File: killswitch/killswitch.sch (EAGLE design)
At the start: 12 parts

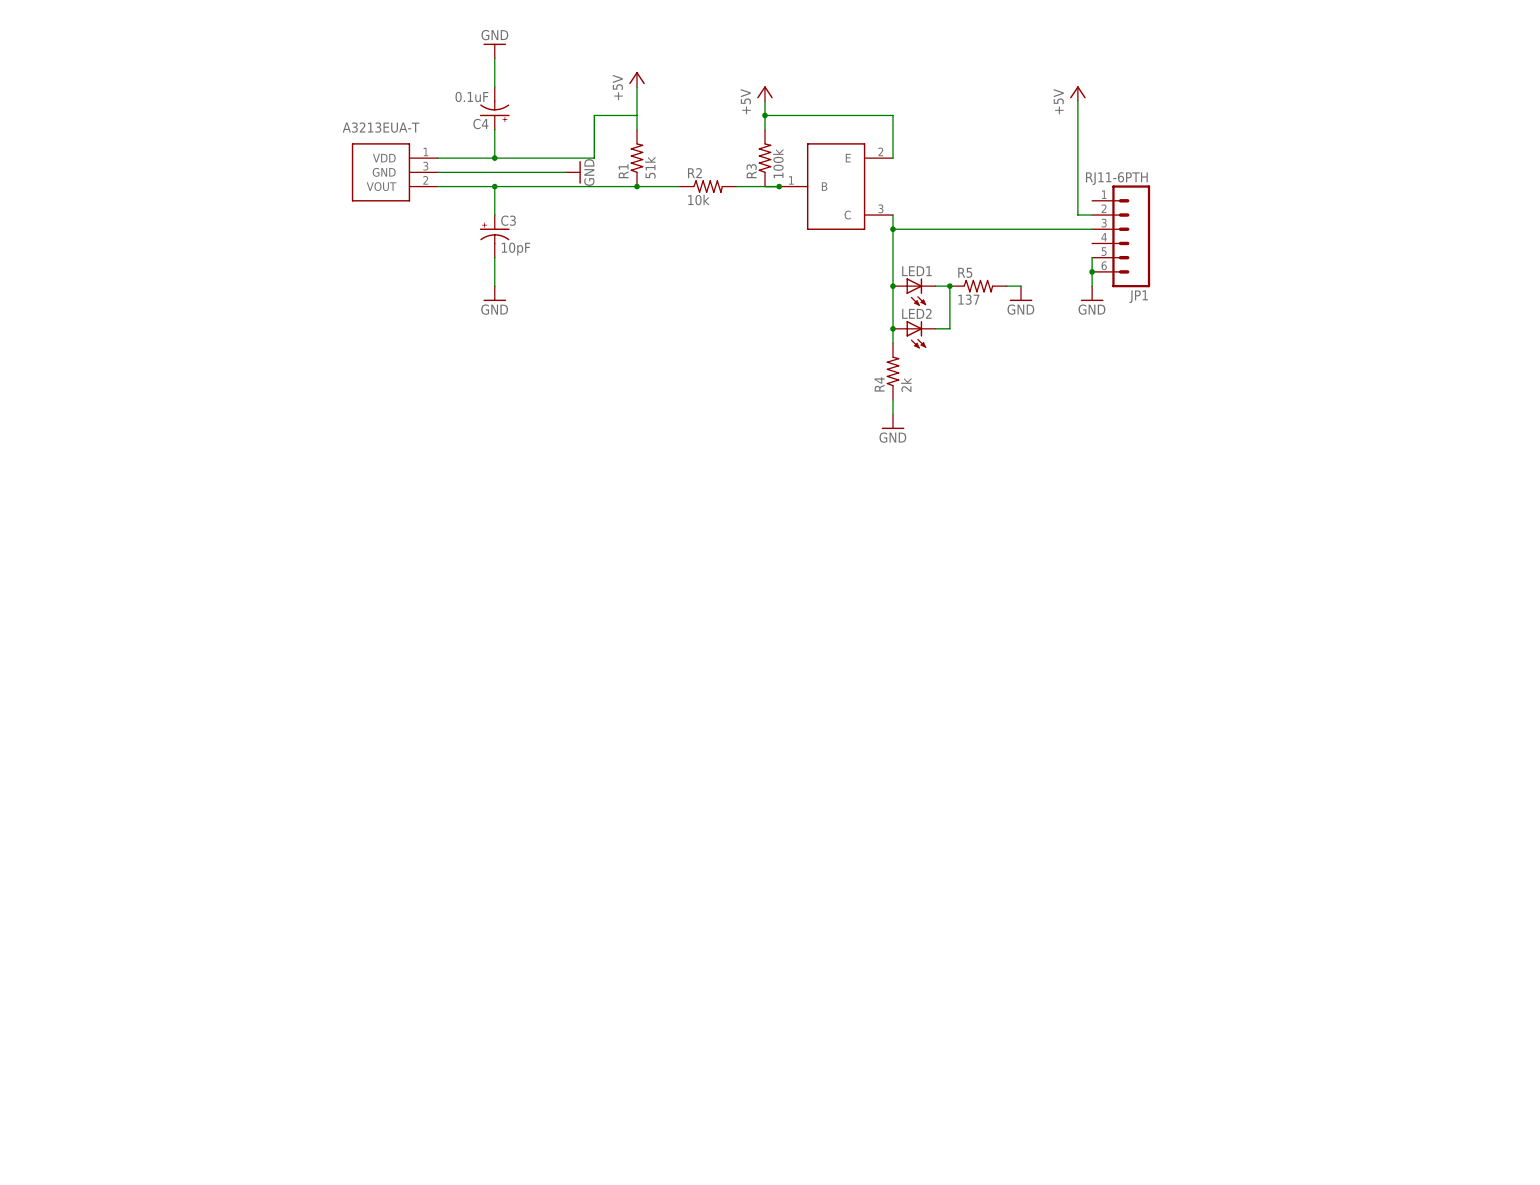
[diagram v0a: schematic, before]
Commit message: Built Schematic and PCB
-Uses 4 open drain, very sensitive hall effects
-The output gets fed into a 4 port NAND gate.
-Output of NAND gate is fed through a buffer.
-Output of HIGH means theres a magnetic field near the board.
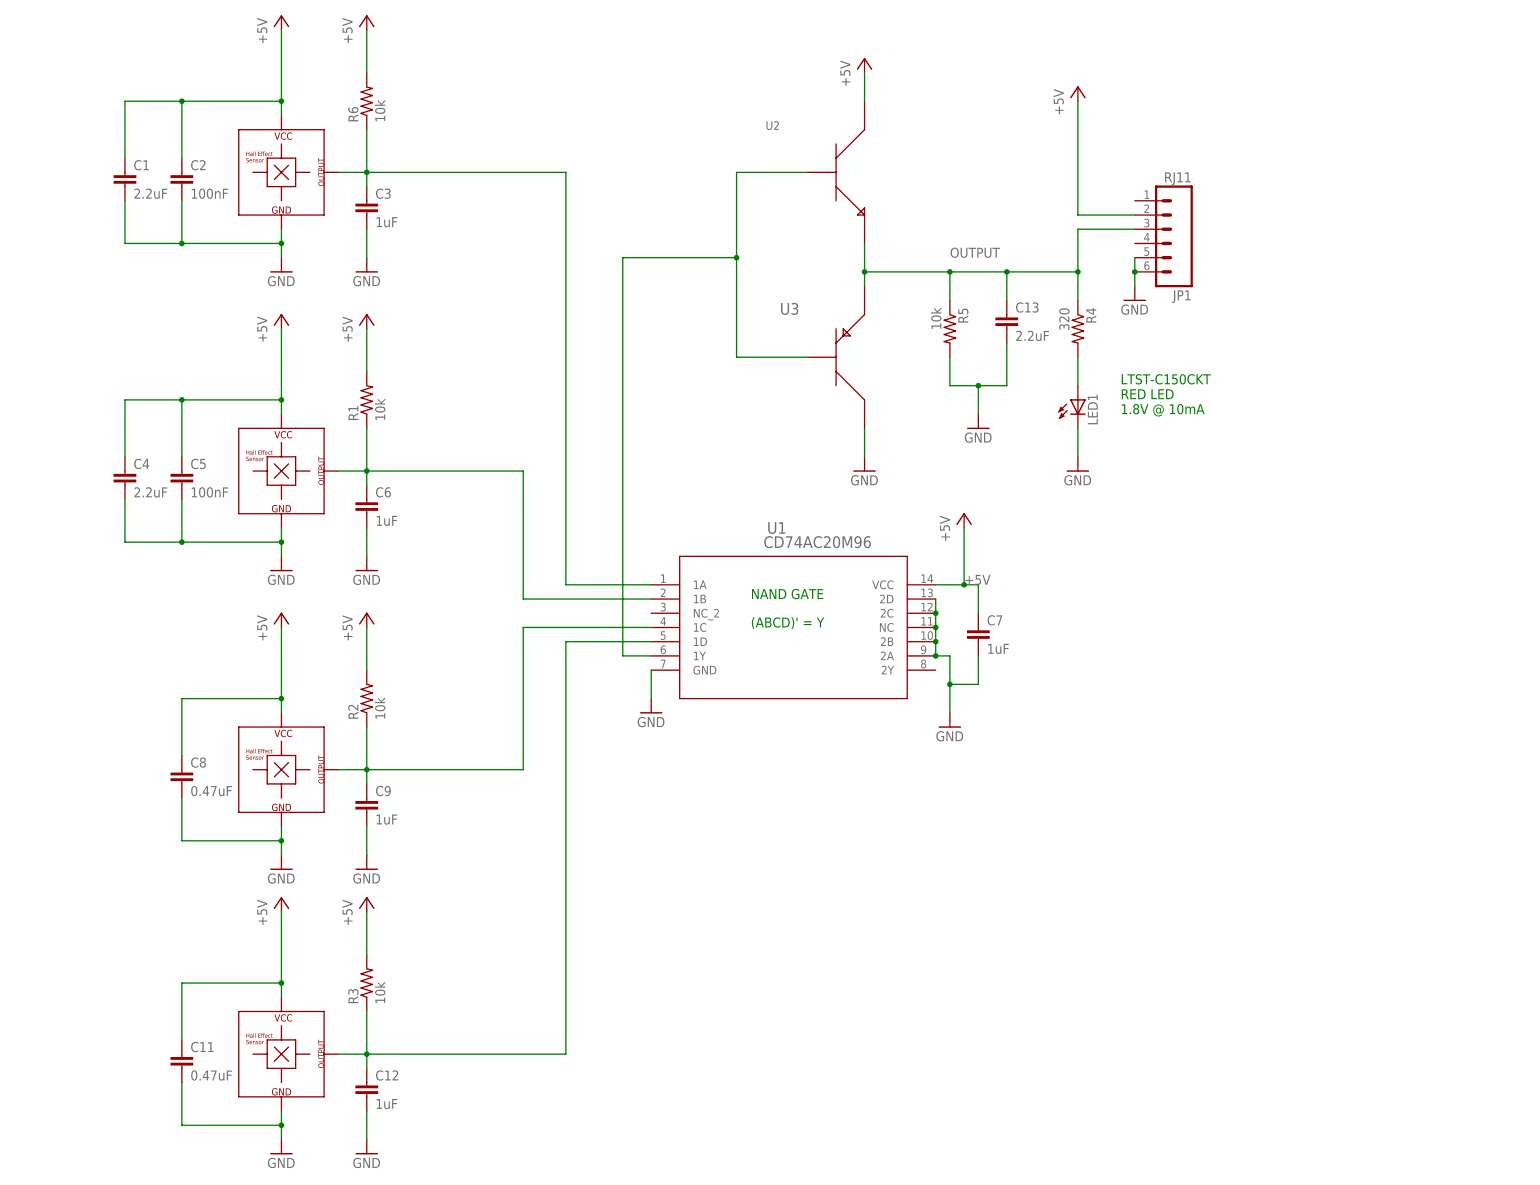
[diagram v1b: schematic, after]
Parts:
- removed LED2: (no value), adafruit:LEDCHIPLED_1206
- added C1, C13: 2.2uF, resistor:C-EUC0805
- added C11, C8: 0.47uF, resistor:C-EUC0603
- added C12, C6, C7, C9: 1uF, resistor:C-EUC0603
- added C2, C5: 100nF, resistor:C-EUC0603
- added R6: 10k, resistor:R-US_R0805
- added U$4, U$5: TCS40DLR, KillSwitch:TCS40DLR
- added U1: CD74AC20M96, KillSwitch:CD74AC20M96
- added U2: MMBT2222ALT1G, KillSwitch:MMBT2222ALT1G
- added U3: MMBT3906LT1G, KillSwitch:MMBT3906LT1G
- C3: value 10pF -> 1uF; device SparkFun:CAP_POL1206 -> resistor:C-EUC0603
- C4: value 0.1uF -> 2.2uF; device SparkFun:CAP_POL1206 -> resistor:C-EUC0805
- JP1: value RJ11-6PTH -> RJ11
- LED1: device adafruit:LEDCHIPLED_1206 -> SparkFun (2015_10_14 22_27_04 UTC):LED1206
- R1: value 51k -> 10k; device SparkFun-Passives:RESISTOR1206 -> resistor:R-US_R0805
- R2: device SparkFun-Passives:RESISTOR1206 -> resistor:R-US_R0805
- R3: value 100k -> 10k; device SparkFun-Passives:RESISTOR1206 -> resistor:R-US_R0805
- R4: value 2k -> 320; device SparkFun:RESISTOR1206 -> resistor:R-US_R0805
- R5: value 137 -> 10k; device SparkFun:RESISTOR1206 -> resistor:R-US_R0805
- U$1: value A3213EUA -> TCS40DLR; device ARVP_killswitch:A3213EUA -> KillSwitch:TCS40DLR
- U$3: value MMBT3906 -> TCS40DLR; device ARVP_killswitch:MMBT3906 -> KillSwitch:TCS40DLR
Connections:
- removed net N$4: JP1.3, LED1.A, LED2.A, R4.2, U$3.C
- new net N$5: C3.1, R6.1, U$1.OUTPUT, U1.1A
- new net N$6: U1.1Y, U2.B, U3.B
- new net N$8: LED1.A, R4.2
- new net OUTPUT: C13.1, JP1.3, R4.1, R5.1, U2.E, U3.E
- net +5V: now also C1.1, C11.1, C2.1, C4.1, C5.1, C7.1, C8.1, R2.2, R6.2, U$1.VCC, U$3.VCC, U$4.VCC, U$5.VCC, U1.VCC, U2.C; no longer C4.+, U$1.VDD, U$3.E
- net GND: now also C1.2, C11.2, C12.2, C13.2, C2.2, C3.2, C4.2, C5.2, C6.2, C7.2, C8.2, C9.2, LED1.C, U$3.GND, U$4.GND, U$5.GND, U1.2A, U1.2B, U1.2C, U1.2D, U1.GND, U1.NC, U3.C; no longer C3.-, C4.-, R4.1
- net N$1: now also C6.1, U$3.OUTPUT, U1.1B; no longer C3.+, R2.1, U$1.VOUT
- net N$2: now also C9.1, R2.1, U$4.OUTPUT, U1.1C; no longer R2.2, R3.1, U$3.B
- net N$3: now also C12.1, R3.1, U$5.OUTPUT, U1.1D; no longer LED1.C, LED2.C, R5.1
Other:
- note added: "(ABCD)' = Y"
- note added: "LTST-C150CKT RED LED 1.8V @ 10mA"
- note added: "NAND GATE"
- moved on the sheet: JP1, LED1, R1, R2, R3, R4, R5

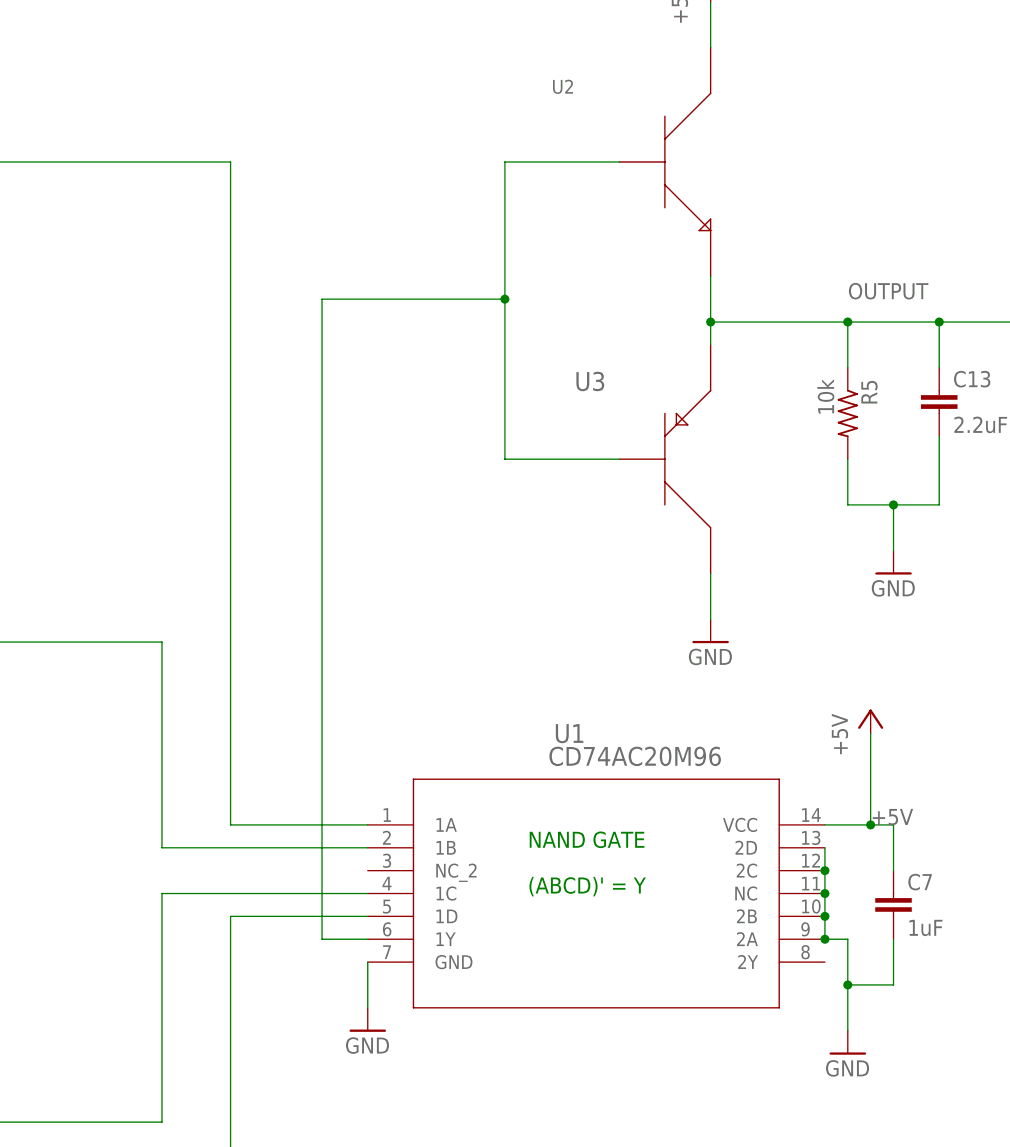
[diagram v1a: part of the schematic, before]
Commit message: Miss spec'ed a part
NAND gate I choose only went up to 3.3V, I swapped it out with one
that'll go up to 5V.
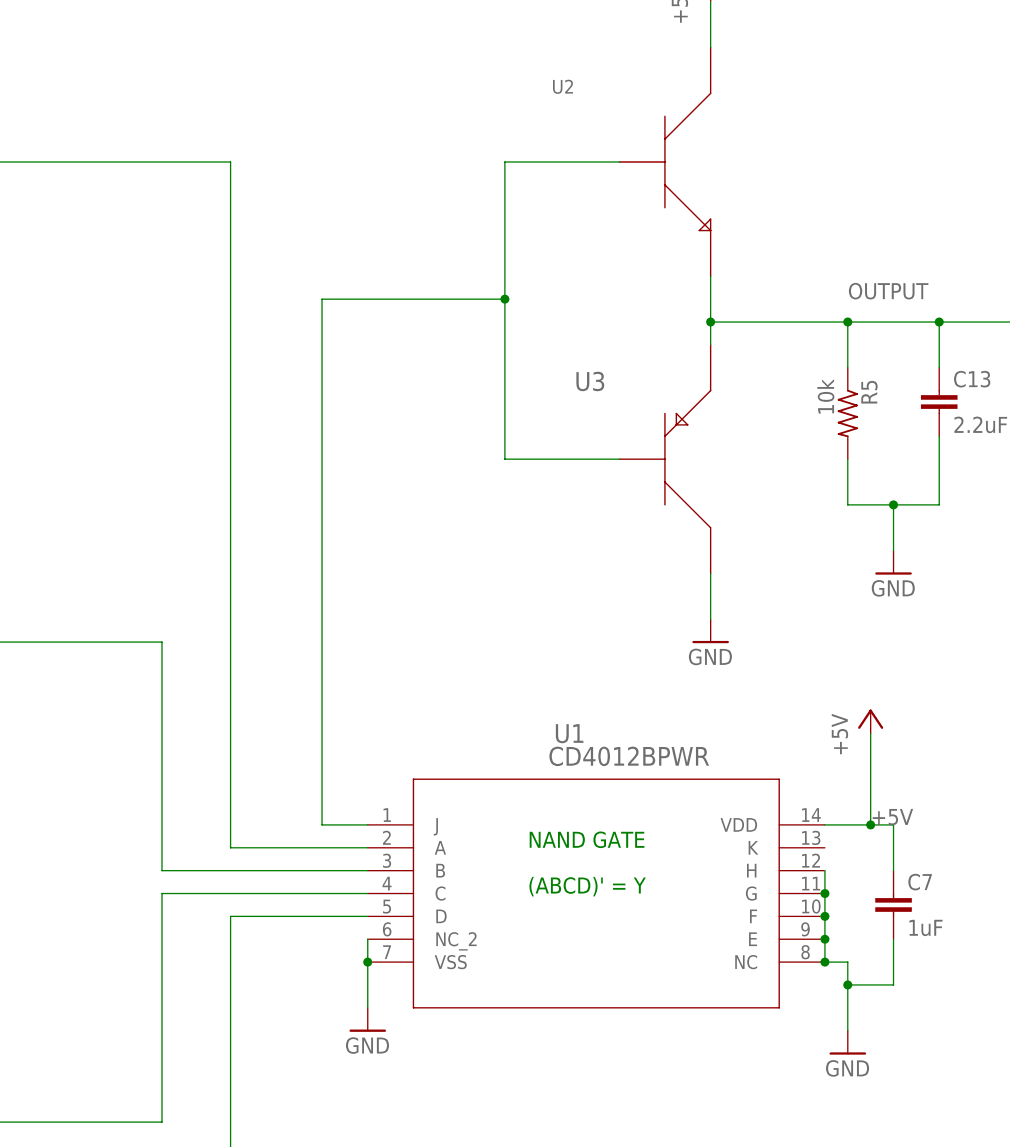
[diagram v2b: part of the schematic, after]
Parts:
- U1: value CD74AC20M96 -> CD4012BPWR; device KillSwitch:CD74AC20M96 -> KillSwitch:CD4012BPWR
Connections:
- net +5V: now also U1.VDD; no longer U1.VCC
- net GND: now also U1.E, U1.F, U1.G, U1.H, U1.NC_2, U1.VSS; no longer U1.2A, U1.2B, U1.2C, U1.2D, U1.GND
- net N$1: now also U1.B; no longer U1.1B
- net N$2: now also U1.C; no longer U1.1C
- net N$3: now also U1.D; no longer U1.1D
- net N$5: now also U1.A; no longer U1.1A
- net N$6: now also U1.J; no longer U1.1Y
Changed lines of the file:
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@@
 <part name="LED1" library="SparkFun (2015_10_14 22_27_04 UTC)" deviceset="LED" device="1206"/>
 <part name="GND14" library="supply1" library_urn="urn:adsk.eagle:library:371" deviceset="GND" device=""/>
-<part name="U1" library="KillSwitch" library_urn="urn:adsk.eagle:library:576207" deviceset="CD74AC20M96" device=""/>
+<part name="U1" library="KillSwitch" library_urn="urn:adsk.eagle:library:576207" deviceset="CD4012BPWR" device=""/>
 </parts>
 <sheets>
@@
 <segment>
 <pinref part="GND10" gate="1" pin="GND"/>
-<pinref part="U1" gate="A" pin="GND"/>
+<pinref part="U1" gate="A" pin="VSS"/>
 <wire x1="38.1" y1="-35.56" x2="38.1" y2="-40.64" width="0.1524" layer="91"/>
+<pinref part="U1" gate="A" pin="NC_2"/>
+<wire x1="38.1" y1="-35.56" x2="38.1" y2="-33.02" width="0.1524" layer="91"/>
+<junction x="38.1" y="-35.56"/>
 </segment>
 <segment>
 <pinref part="GND11" gate="1" pin="GND"/>
 <pinref part="C7" gate="G$1" pin="2"/>
-<wire x1="91.44" y1="-38.1" x2="91.44" y2="-43.18" width="0.1524" layer="91"/>
 <wire x1="96.52" y1="-33.02" x2="96.52" y2="-38.1" width="0.1524" layer="91"/>
 <wire x1="96.52" y1="-38.1" x2="91.44" y2="-38.1" width="0.1524" layer="91"/>
-<pinref part="U1" gate="A" pin="2A"/>
-<pinref part="U1" gate="A" pin="2B"/>
-<pinref part="U1" gate="A" pin="NC"/>
-<pinref part="U1" gate="A" pin="2C"/>
-<pinref part="U1" gate="A" pin="2D"/>
-<wire x1="88.9" y1="-22.86" x2="88.9" y2="-25.4" width="0.1524" layer="91"/>
-<junction x="88.9" y="-25.4"/>
+<wire x1="91.44" y1="-38.1" x2="91.44" y2="-43.18" width="0.1524" layer="91"/>
+<pinref part="U1" gate="A" pin="E"/>
+<pinref part="U1" gate="A" pin="F"/>
+<pinref part="U1" gate="A" pin="G"/>
+<pinref part="U1" gate="A" pin="H"/>
 <wire x1="88.9" y1="-25.4" x2="88.9" y2="-27.94" width="0.1524" layer="91"/>
 <junction x="88.9" y="-27.94"/>
@@
 <junction x="88.9" y="-30.48"/>
 <wire x1="88.9" y1="-30.48" x2="88.9" y2="-33.02" width="0.1524" layer="91"/>
-<wire x1="88.9" y1="-33.02" x2="91.44" y2="-33.02" width="0.1524" layer="91"/>
-<wire x1="91.44" y1="-33.02" x2="91.44" y2="-38.1" width="0.1524" layer="91"/>
 <junction x="88.9" y="-33.02"/>
+<pinref part="U1" gate="A" pin="NC"/>
+<wire x1="88.9" y1="-35.56" x2="88.9" y2="-33.02" width="0.1524" layer="91"/>
+<wire x1="88.9" y1="-35.56" x2="91.44" y2="-35.56" width="0.1524" layer="91"/>
+<wire x1="91.44" y1="-35.56" x2="91.44" y2="-38.1" width="0.1524" layer="91"/>
+<junction x="88.9" y="-35.56"/>
 <junction x="91.44" y="-38.1"/>
 </segment>
@@
 <wire x1="96.52" y1="-20.32" x2="96.52" y2="-25.4" width="0.1524" layer="91"/>
 <junction x="93.98" y="-20.32"/>
-<pinref part="U1" gate="A" pin="VCC"/>
+<pinref part="U1" gate="A" pin="VDD"/>
 </segment>
 <segment>
@@
 <junction x="-12.7" y="53.34"/>
 <wire x1="-12.7" y1="53.34" x2="22.86" y2="53.34" width="0.1524" layer="91"/>
-<wire x1="22.86" y1="53.34" x2="22.86" y2="-20.32" width="0.1524" layer="91"/>
-<pinref part="U1" gate="A" pin="1A"/>
-<wire x1="22.86" y1="-20.32" x2="38.1" y2="-20.32" width="0.1524" layer="91"/>
+<wire x1="22.86" y1="53.34" x2="22.86" y2="-22.86" width="0.1524" layer="91"/>
+<pinref part="U1" gate="A" pin="A"/>
+<wire x1="22.86" y1="-22.86" x2="38.1" y2="-22.86" width="0.1524" layer="91"/>
 </segment>
 </net>
@@
 <junction x="-12.7" y="0"/>
 <wire x1="-12.7" y1="0" x2="15.24" y2="0" width="0.1524" layer="91"/>
-<wire x1="15.24" y1="0" x2="15.24" y2="-22.86" width="0.1524" layer="91"/>
-<pinref part="U1" gate="A" pin="1B"/>
-<wire x1="15.24" y1="-22.86" x2="38.1" y2="-22.86" width="0.1524" layer="91"/>
+<wire x1="15.24" y1="0" x2="15.24" y2="-25.4" width="0.1524" layer="91"/>
+<pinref part="U1" gate="A" pin="B"/>
+<wire x1="15.24" y1="-25.4" x2="38.1" y2="-25.4" width="0.1524" layer="91"/>
 </segment>
 </net>
@@
 <wire x1="15.24" y1="-53.34" x2="15.24" y2="-27.94" width="0.1524" layer="91"/>
 <wire x1="15.24" y1="-27.94" x2="38.1" y2="-27.94" width="0.1524" layer="91"/>
-<pinref part="U1" gate="A" pin="1C"/>
+<pinref part="U1" gate="A" pin="C"/>
 </segment>
 </net>
@@
 <wire x1="22.86" y1="-104.14" x2="22.86" y2="-30.48" width="0.1524" layer="91"/>
 <wire x1="22.86" y1="-30.48" x2="38.1" y2="-30.48" width="0.1524" layer="91"/>
-<pinref part="U1" gate="A" pin="1D"/>
+<pinref part="U1" gate="A" pin="D"/>
 </segment>
 </net>
 <net name="N$6" class="0">
 <segment>
-<wire x1="33.02" y1="-33.02" x2="33.02" y2="38.1" width="0.1524" layer="91"/>
+<wire x1="33.02" y1="-20.32" x2="33.02" y2="38.1" width="0.1524" layer="91"/>
 <pinref part="U3" gate="A" pin="B"/>
 <wire x1="66.04" y1="20.32" x2="53.34" y2="20.32" width="0.1524" layer="91"/>
@@
 <junction x="53.34" y="38.1"/>
 <wire x1="33.02" y1="38.1" x2="53.34" y2="38.1" width="0.1524" layer="91"/>
-<pinref part="U1" gate="A" pin="1Y"/>
-<wire x1="33.02" y1="-33.02" x2="38.1" y2="-33.02" width="0.1524" layer="91"/>
-</segment>
-</net>
+<pinref part="U1" gate="A" pin="J"/>
+<wire x1="33.02" y1="-20.32" x2="38.1" y2="-20.32" width="0.1524" layer="91"/>
+</segment>
+</net>
